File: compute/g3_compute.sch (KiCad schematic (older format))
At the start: 37 parts, among them J1 CPPC_Conn, J101 CONSMA001-SMD-G, J102 Temp_Connector_1x4, J3 GPIO_Breakout_Conn, U101 PA1616D, U102 LoRa-E5

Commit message: Adding Power to compute connector
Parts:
- removed J?: Conn_Power_Compute_01x10_Male, symbol Connector:Conn_01x10_Male
- added J?: Conn_Power_Compute_01x10_Female, symbol Connector:Conn_01x10_Female
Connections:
- wire segments 177 -> 174
- no-connect marks 0 -> 1
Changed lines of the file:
@@
 Wire Wire Line
 	4850 2975 4450 2975
-Wire Wire Line
-	6650 1875 6750 1875
-Wire Wire Line
-	6650 1975 6750 1975
-Wire Wire Line
-	6750 1975 6750 1875
-Connection ~ 6750 1875
-Wire Wire Line
-	6750 1875 7025 1875
 Text GLabel 7025 1875 2    50   Input ~ 0
 5V
@@
 Text Notes 8550 6400 0    50   ~ 0
 CPPC Breakout Points
-Text Notes 6800 6325 0    50   ~ 0
+Text Notes 7300 6375 0    50   ~ 0
 Power Subsystem Points
 Wire Notes Line
@@
 Wire Notes Line
 	7625 675  9600 675
-$Comp
-L Connector:Conn_01x10_Male J?
-U 1 1 61FDC30C
-P 6675 5450
-F 0 "J?" H 6425 5925 50  0000 C CNN
-F 1 "Conn_Power_Compute_01x10_Male" H 7025 6000 50  0000 C CNN
-F 2 "" H 6675 5450 50  0001 C CNN
-F 3 "~" H 6675 5450 50  0001 C CNN
-	1    6675 5450
-	1    0    0    -1
-$EndComp
-Wire Wire Line
-	6875 5050 7400 5050
-Wire Wire Line
-	6875 5150 7325 5150
-Wire Wire Line
-	6875 5250 7325 5250
-Wire Wire Line
-	6875 5350 7325 5350
-Wire Wire Line
-	6875 5450 7325 5450
-Wire Wire Line
-	6875 5550 7325 5550
-Wire Wire Line
-	6875 5650 7400 5650
-Wire Wire Line
-	6875 5750 7400 5750
-Wire Wire Line
-	6875 5850 7325 5850
-Wire Wire Line
-	6875 5950 7300 5950
-Text Label 7325 5350 2    50   ~ 0
+Text Label 7825 5375 2    50   ~ 0
 ~PS_CC_CE
-Text Label 7325 5250 2    50   ~ 0
-~PS_CC_INT
-Text Label 7325 5850 2    50   ~ 0
+Text Label 7825 5875 2    50   ~ 0
 PS_VR_PS
-Text Label 7325 5150 2    50   ~ 0
+Text Label 7825 5175 2    50   ~ 0
 ~PS_CC_QON
-Text GLabel 7400 5050 2    50   Output ~ 0
-5V
 $Comp
 L power:GND #PWR?
 U 1 1 62071DF4
-P 7300 6025
-F 0 "#PWR?" H 7300 5775 50  0001 C CNN
-F 1 "GND" H 7305 5852 50  0000 C CNN
-F 2 "" H 7300 6025 50  0001 C CNN
-F 3 "" H 7300 6025 50  0001 C CNN
-	1    7300 6025
-	1    0    0    -1
-$EndComp
-Wire Wire Line
-	7300 5950 7300 6025
-Text Label 7325 5450 2    50   ~ 0
+P 7825 6050
+F 0 "#PWR?" H 7825 5800 50  0001 C CNN
+F 1 "GND" H 7830 5877 50  0000 C CNN
+F 2 "" H 7825 6050 50  0001 C CNN
+F 3 "" H 7825 6050 50  0001 C CNN
+	1    7825 6050
+	1    0    0    -1
+$EndComp
+Wire Wire Line
+	7825 5975 7825 6050
+Text Label 7825 5475 2    50   ~ 0
 PS_CC_SCL
-Text Label 7325 5550 2    50   ~ 0
+Text Label 7825 5575 2    50   ~ 0
 PS_CC_SDA
-Text GLabel 7400 5650 2    50   Output ~ 0
-VSolSense
-Text GLabel 7400 5750 2    50   Output ~ 0
+Text GLabel 7375 5775 0    50   Output ~ 0
 VBatSense
 Wire Notes Line
@@
 Wire Notes Line
 	7375 4475 11125 4475
-Wire Notes Line
-	5550 6450 6750 6450
-Wire Notes Line
-	5550 7700 5550 6450
-Wire Notes Line
-	6750 7700 5550 7700
-Wire Notes Line
-	6750 6450 6750 7700
+Wire Wire Line
+	9275 1675 10575 1675
+Wire Wire Line
+	10525 1875 10525 3575
+Wire Notes Line
+	2575 4550 2575 7725
+Wire Notes Line
+	5225 4550 5225 7725
+Wire Wire Line
+	1825 900  1575 900
+Wire Wire Line
+	6650 1875 7025 1875
+NoConn ~ 6650 1975
+Wire Wire Line
+	6350 6700 5950 6700
+Wire Wire Line
+	6350 6800 5950 6800
+Wire Wire Line
+	6350 6900 5950 6900
+Wire Wire Line
+	6350 7000 5950 7000
+Wire Wire Line
+	6350 7100 5950 7100
+Wire Wire Line
+	6350 7200 5950 7200
+Wire Wire Line
+	6350 7300 5950 7300
+Wire Wire Line
+	6350 7400 5950 7400
+Wire Wire Line
+	6350 7500 5950 7500
+Text Label 5950 6700 0    50   ~ 0
+PI_GPIO4
+Text Label 5950 6900 0    50   ~ 0
+PI_GPIO17
+Text Label 5950 7500 0    50   ~ 0
+PI_GPIO27
+Text Label 5950 7100 0    50   ~ 0
+PI_GPIO22
+Text Label 5950 7000 0    50   ~ 0
+PI_GPIO18
+Text Label 5950 7200 0    50   ~ 0
+PI_GPIO23
+Text Label 5950 7300 0    50   ~ 0
+PI_GPIO24
+Text Label 5950 7400 0    50   ~ 0
+PI_GPIO25
+Text Label 5950 6800 0    50   ~ 0
+PI_GPIO7
+Text Notes 5850 7650 0    50   ~ 0
+GPIO Breakout Points
 $Comp
 L Connector:Conn_01x09_Female J3
@@
 	1    0    0    -1
 $EndComp
-Text Notes 5850 7650 0    50   ~ 0
-GPIO Breakout Points
-Text Label 5950 6800 0    50   ~ 0
-PI_GPIO7
-Text Label 5950 7400 0    50   ~ 0
-PI_GPIO25
-Text Label 5950 7300 0    50   ~ 0
-PI_GPIO24
-Text Label 5950 7200 0    50   ~ 0
-PI_GPIO23
-Text Label 5950 7000 0    50   ~ 0
-PI_GPIO18
-Text Label 5950 7100 0    50   ~ 0
-PI_GPIO22
-Text Label 5950 7500 0    50   ~ 0
-PI_GPIO27
-Text Label 5950 6900 0    50   ~ 0
-PI_GPIO17
-Text Label 5950 6700 0    50   ~ 0
-PI_GPIO4
-Wire Wire Line
-	6350 7500 5950 7500
-Wire Wire Line
-	6350 7400 5950 7400
-Wire Wire Line
-	6350 7300 5950 7300
-Wire Wire Line
-	6350 7200 5950 7200
-Wire Wire Line
-	6350 7100 5950 7100
-Wire Wire Line
-	6350 7000 5950 7000
-Wire Wire Line
-	6350 6900 5950 6900
-Wire Wire Line
-	6350 6800 5950 6800
-Wire Wire Line
-	6350 6700 5950 6700
-Wire Wire Line
-	9275 1675 10575 1675
-Wire Wire Line
-	10525 1875 10525 3575
-Wire Notes Line
-	2575 4550 2575 7725
-Wire Notes Line
-	5225 4550 5225 7725
-Wire Wire Line
-	1825 900  1575 900
+Wire Notes Line
+	6750 6450 6750 7700
+Wire Notes Line
+	6750 7700 5550 7700
+Wire Notes Line
+	5550 7700 5550 6450
+Wire Notes Line
+	5550 6450 6750 6450
+Wire Wire Line
+	7325 5075 7925 5075
+Text GLabel 7325 5075 0    50   Output ~ 0
+5V
+Text Label 7825 5275 2    50   ~ 0
+~PS_CC_INT
+$Comp
+L Connector:Conn_01x10_Female J?
+U 1 1 61D84775
+P 8125 5475
+F 0 "J?" H 6700 5925 50  0000 L CNN
+F 1 "Conn_Power_Compute_01x10_Female" H 6700 6025 50  0000 L CNN
+F 2 "" H 8125 5475 50  0001 C CNN
+F 3 "~" H 8125 5475 50  0001 C CNN
+	1    8125 5475
+	1    0    0    -1
+$EndComp
+Wire Wire Line
+	7825 5275 7925 5275
+Wire Wire Line
+	7825 5175 7925 5175
+Wire Wire Line
+	7925 5375 7825 5375
+Wire Wire Line
+	7825 5475 7925 5475
+Wire Wire Line
+	7825 5575 7925 5575
+Wire Wire Line
+	7925 5875 7825 5875
+Wire Wire Line
+	7375 5775 7925 5775
+Wire Wire Line
+	7925 5975 7825 5975
+Wire Wire Line
+	7375 5675 7925 5675
+Text GLabel 7375 5675 0    50   Output ~ 0
+VSolSense
+Wire Notes Line
+	6675 4850 8275 4850
+Wire Notes Line
+	8275 4850 8275 6400
+Wire Notes Line
+	8275 6400 6675 6400
+Wire Notes Line
+	6675 6400 6675 4850
 $EndSCHEMATC

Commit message: Adjusting board connectors
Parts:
- removed J1: CPPC_Conn, Connector_Samtec_HLE_SMD:Samtec_HLE-103-02-xxx-DV_2x03_P2.54mm_Horizontal, symbol Connector:Conn_01x06_Female
- removed J?: Conn_Power_Compute_01x10_Female, symbol Connector:Conn_01x10_Female
- added J103: Conn_02x03_Counter_Clockwise, symbol Connector_Generic:Conn_02x03_Counter_Clockwise
- added J104: Conn_Power_Compute_02x05, symbol Connector_Generic:Conn_02x05_Counter_Clockwise
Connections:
- net labels added: PS_VSolSense
- net labels removed: VBatSense, VSolSense
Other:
- note removed: "CPPC Breakout Points"
- note removed: "Power Subsystem Points"
- moved on the sheet: J3

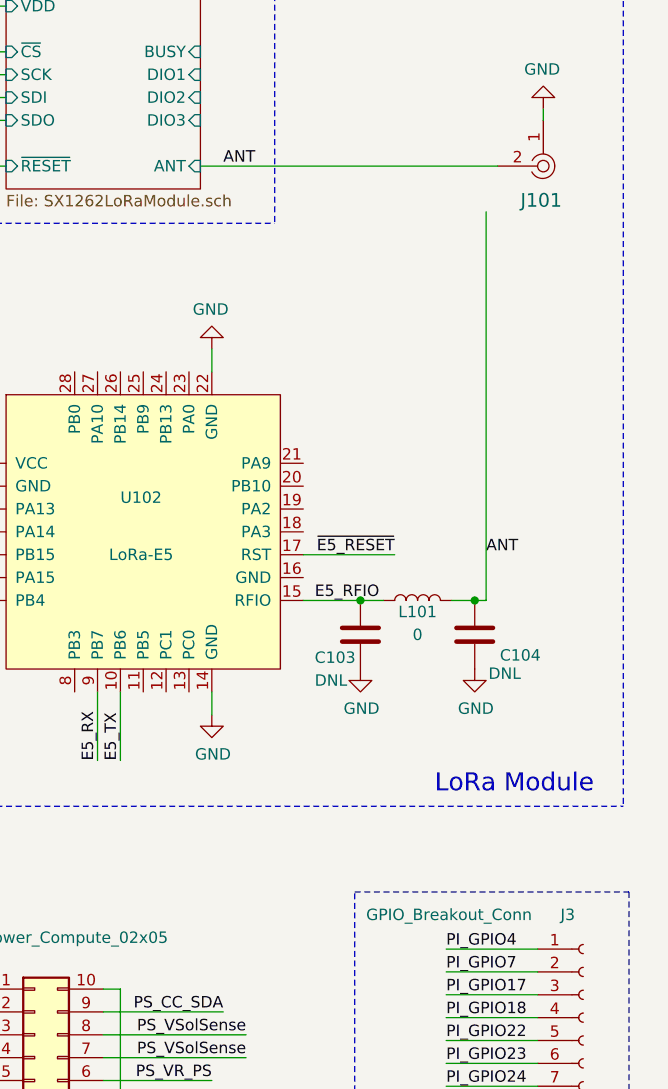
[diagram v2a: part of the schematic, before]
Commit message: Adjusting connectors foot prints
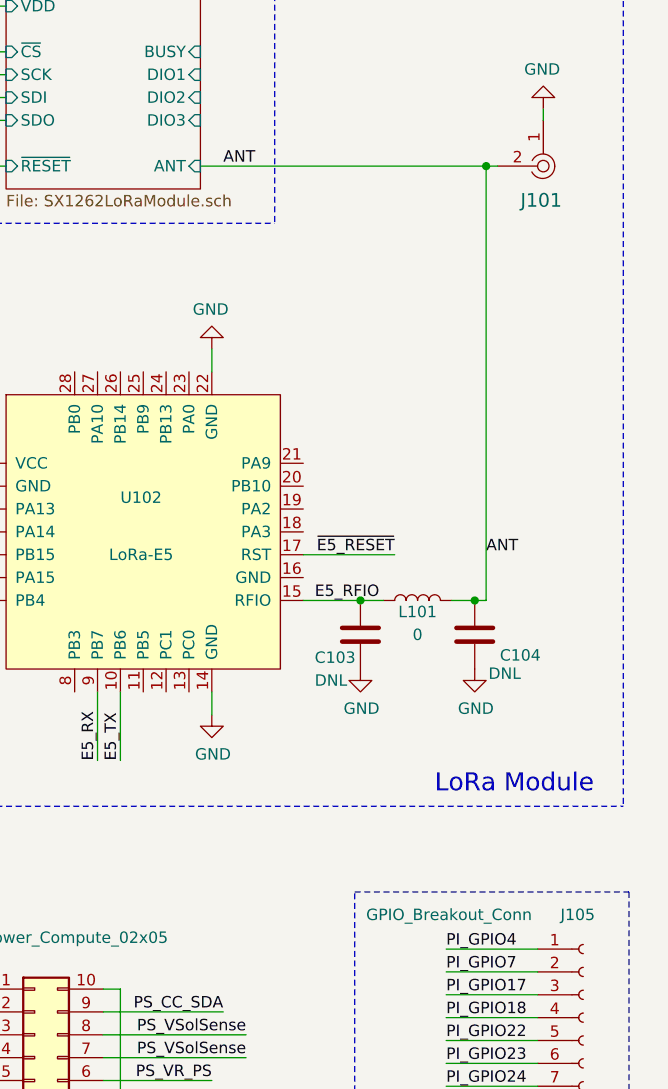
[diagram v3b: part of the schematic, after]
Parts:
- J103: footprint (none) -> Connector_Samtec_HLE_SMD:Samtec_HLE-103-02-xxx-DV_2x03_P2.54mm_Horizontal
- J104: footprint (none) -> Connector_Samtec_HLE_SMD:Samtec_HLE-105-02-xxx-DV_2x05_P2.54mm_Horizontal
- renumbered J3 to J105
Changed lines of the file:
@@
 	7375 4475 11125 4475
 Wire Wire Line
-	9275 1675 10575 1675
-Wire Wire Line
-	10525 1875 10525 3575
+	9275 1675 10525 1675
 Wire Notes Line
 	2575 4550 2575 7725
@@
 GPIO Breakout Points
 $Comp
-L Connector:Conn_01x09_Female J3
+L Connector:Conn_01x09_Female J105
 U 1 1 61D95581
 P 10950 5500
-F 0 "J3" H 10850 6050 50  0000 L CNN
+F 0 "J105" H 10850 6050 50  0000 L CNN
 F 1 "GPIO_Breakout_Conn" H 10000 6050 50  0000 L CNN
 F 2 "Connector_Samtec_HLE_SMD:Samtec_HLE-105-02-xxx-DV_2x05_P2.54mm_Horizontal" H 10950 5500 50  0001 C CNN
@@
 F 0 "J103" H 6000 5725 50  0000 C CNN
 F 1 "Conn_02x03_Counter_Clockwise" H 6550 5800 50  0000 C CNN
-F 2 "" H 6525 5450 50  0001 C CNN
+F 2 "Connector_Samtec_HLE_SMD:Samtec_HLE-103-02-xxx-DV_2x03_P2.54mm_Horizontal" H 6525 5450 50  0001 C CNN
 F 3 "~" H 6525 5450 50  0001 C CNN
 	1    6525 5450
@@
 F 0 "J104" H 8125 5825 50  0000 C CNN
 F 1 "Conn_Power_Compute_02x05" H 8625 5900 50  0000 C CNN
-F 2 "" H 8550 5475 50  0001 C CNN
+F 2 "Connector_Samtec_HLE_SMD:Samtec_HLE-105-02-xxx-DV_2x05_P2.54mm_Horizontal" H 8550 5475 50  0001 C CNN
 F 3 "~" H 8550 5475 50  0001 C CNN
 	1    8550 5475
@@
 Wire Wire Line
 	6900 5350 6900 5650
+Wire Wire Line
+	10525 1675 10525 3575
+Connection ~ 10525 1675
+Wire Wire Line
+	10525 1675 10575 1675
 $EndSCHEMATC
